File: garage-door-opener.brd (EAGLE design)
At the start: 54.3 x 47.6 mm, 17 parts, among them IC1 LM2575-3.3T, K1 RR1A, T1 BC547, U1 ESP8266, X2 Connector

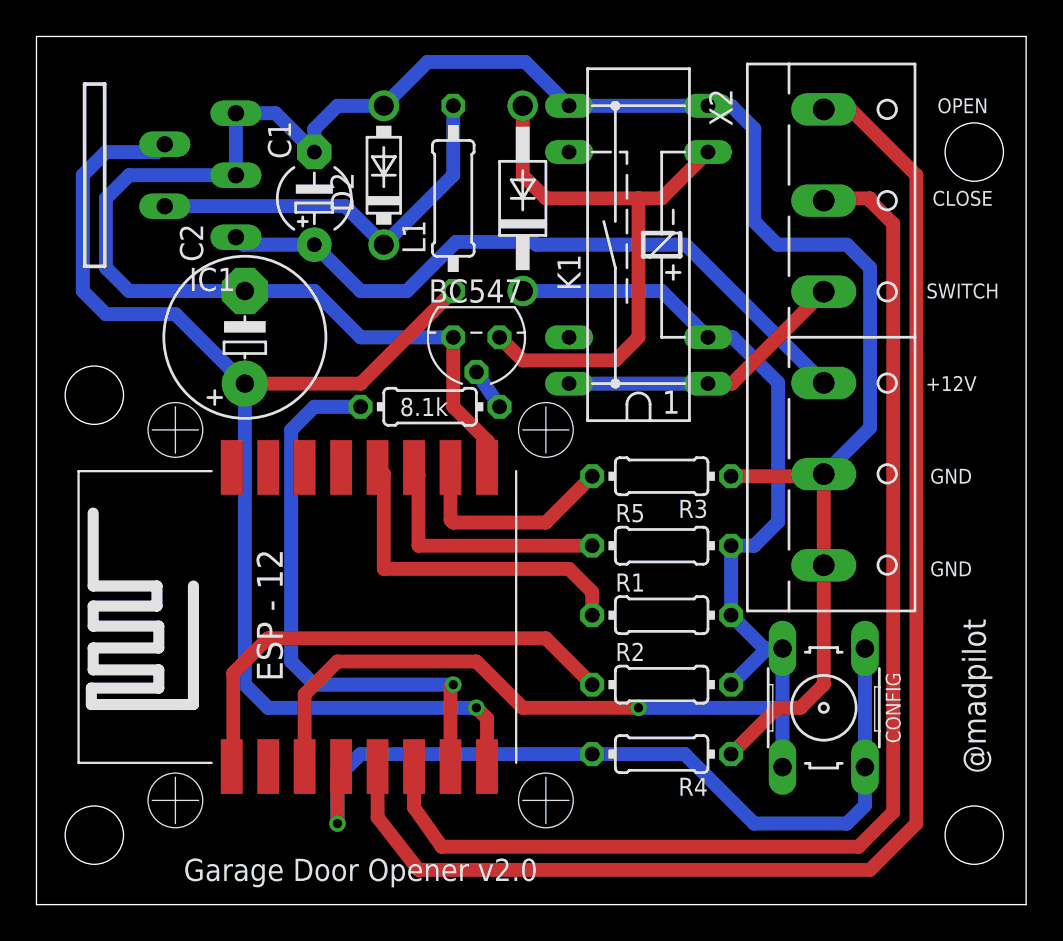
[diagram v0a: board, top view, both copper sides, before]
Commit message: Aligning resistors properly
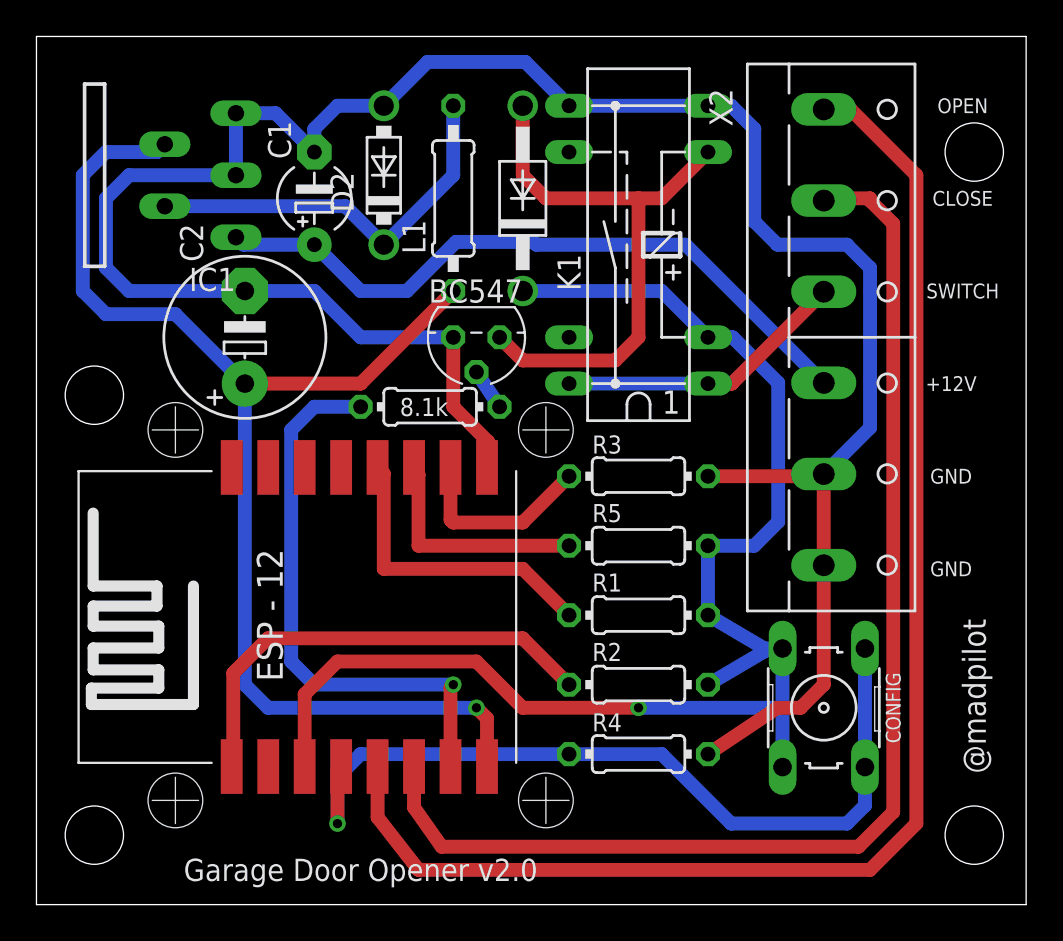
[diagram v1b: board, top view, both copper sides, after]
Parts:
- moved R1 1.27 mm to (33.0, 52.1)
- moved R2 1.27 mm to (33.0, 48.3)
- moved R3 1.27 mm to (33.0, 59.7)
- moved R4 1.27 mm to (33.0, 44.5)
- moved R5 1.27 mm to (33.0, 55.9)
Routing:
- net VCC: track 75.4 -> 78.7 mm
- net GND: track 125.2 -> 127.5 mm
- net N$7: track 18.9 -> 16.9 mm
- net N$8: track 26.7 -> 25.4 mm
- net N$6: track 11.8 -> 10.5 mm
- net N$13: track 13.9 -> 12.6 mm
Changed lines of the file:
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@@
 <attribute name="SPICEPREFIX" value="L" x="22.86" y="74.93" size="0.6096" layer="27" rot="R90" display="off"/>
 </element>
-<element name="R1" library="resistor" library_urn="urn:adsk.eagle:library:348" package="0204/7" package3d_urn="urn:adsk.eagle:package:25945/1" value="3k3" x="34.29" y="52.07"/>
-<element name="R2" library="resistor" library_urn="urn:adsk.eagle:library:348" package="0204/7" package3d_urn="urn:adsk.eagle:package:25945/1" value="3k3" x="34.29" y="48.26"/>
-<element name="R3" library="resistor" library_urn="urn:adsk.eagle:library:348" package="0204/7" package3d_urn="urn:adsk.eagle:package:25945/1" value="3k3" x="34.29" y="59.69" rot="R180"/>
+<element name="R1" library="resistor" library_urn="urn:adsk.eagle:library:348" package="0204/7" package3d_urn="urn:adsk.eagle:package:25945/1" value="3k3" x="33.02" y="52.07"/>
+<element name="R2" library="resistor" library_urn="urn:adsk.eagle:library:348" package="0204/7" package3d_urn="urn:adsk.eagle:package:25945/1" value="3k3" x="33.02" y="48.26"/>
+<element name="R3" library="resistor" library_urn="urn:adsk.eagle:library:348" package="0204/7" package3d_urn="urn:adsk.eagle:package:25945/1" value="3k3" x="33.02" y="59.69" smashed="yes" rot="R180">
+<attribute name="NAME" x="30.48" y="60.9346" size="0.9906" layer="25" ratio="10" rot="R180" align="top-right"/>
+<attribute name="VALUE" x="34.6456" y="60.1726" size="0.9906" layer="27" ratio="10" rot="R180"/>
+</element>
 <element name="K1" library="relay" library_urn="urn:adsk.eagle:library:339" package="RR1A" package3d_urn="urn:adsk.eagle:package:24316/1" value="RR1A" x="33.02" y="72.39" rot="R90">
 <attribute name="MF" value="" x="33.02" y="72.39" size="0.6096" layer="27" rot="R90" display="off"/>
@@
 <attribute name="OC_NEWARK" value="36M3542" x="43.18" y="46.99" size="0.6096" layer="27" rot="R90" display="off"/>
 </element>
-<element name="R4" library="resistor" library_urn="urn:adsk.eagle:library:348" package="0204/7" package3d_urn="urn:adsk.eagle:package:25945/1" value="3k3" x="34.29" y="44.45" rot="R180"/>
-<element name="R5" library="resistor" library_urn="urn:adsk.eagle:library:348" package="0204/7" package3d_urn="urn:adsk.eagle:package:25945/1" value="3k3" x="34.29" y="55.88"/>
+<element name="R4" library="resistor" library_urn="urn:adsk.eagle:library:348" package="0204/7" package3d_urn="urn:adsk.eagle:package:25945/1" value="3k3" x="33.02" y="44.45" smashed="yes" rot="R180">
+<attribute name="NAME" x="30.48" y="45.6946" size="0.9906" layer="25" ratio="10" rot="R180" align="top-right"/>
+<attribute name="VALUE" x="34.6456" y="44.9326" size="0.9906" layer="27" ratio="10" rot="R180"/>
+</element>
+<element name="R5" library="resistor" library_urn="urn:adsk.eagle:library:348" package="0204/7" package3d_urn="urn:adsk.eagle:package:25945/1" value="3k3" x="33.02" y="55.88" smashed="yes">
+<attribute name="NAME" x="30.48" y="57.1754" size="0.9906" layer="25" ratio="10"/>
+<attribute name="VALUE" x="31.3944" y="55.3974" size="0.9906" layer="27" ratio="10"/>
+</element>
 </elements>
 <signals>
@@
 <wire x1="15.24" y1="69.85" x2="17.78" y2="67.31" width="0.762" layer="16"/>
 <wire x1="17.78" y1="67.31" x2="22.86" y2="67.31" width="0.762" layer="16"/>
-<wire x1="38.1" y1="59.69" x2="43.18" y2="59.69" width="0.762" layer="1"/>
-<wire x1="38.1" y1="44.45" x2="40.64" y2="46.99" width="0.762" layer="1"/>
+<wire x1="36.83" y1="59.69" x2="43.18" y2="59.69" width="0.762" layer="1"/>
+<wire x1="36.83" y1="44.45" x2="40.64" y2="46.99" width="0.762" layer="1"/>
 <wire x1="40.64" y1="46.99" x2="41.91" y2="46.99" width="0.762" layer="1"/>
 <wire x1="41.91" y1="46.99" x2="43.18" y2="48.26" width="0.762" layer="1"/>
@@
 <contactref element="R5" pad="2"/>
 <wire x1="40.9194" y1="46.99" x2="40.9194" y2="43.7388" width="0.762" layer="16"/>
-<wire x1="38.1" y1="55.88" x2="38.1" y2="52.07" width="0.762" layer="16"/>
-<wire x1="38.1" y1="52.07" x2="39.9288" y2="50.2412" width="0.762" layer="16"/>
+<wire x1="36.83" y1="55.88" x2="36.83" y2="52.07" width="0.762" layer="16"/>
+<wire x1="36.83" y1="52.07" x2="39.9288" y2="50.2412" width="0.762" layer="16"/>
 <wire x1="39.9288" y1="50.2412" x2="40.9194" y2="50.2412" width="0.762" layer="16"/>
-<wire x1="38.1" y1="55.88" x2="39.37" y2="55.88" width="0.762" layer="16"/>
+<wire x1="36.83" y1="55.88" x2="39.37" y2="55.88" width="0.762" layer="16"/>
 <wire x1="40.68" y1="57.19" x2="40.68" y2="64.81" width="0.762" layer="16"/>
 <wire x1="39.37" y1="55.88" x2="40.68" y2="57.19" width="0.762" layer="16"/>
@@
 <via x="33.02" y="46.99" extent="1-16" drill="0.508"/>
 <wire x1="33.02" y1="46.99" x2="40.9194" y2="46.99" width="0.762" layer="16"/>
-<wire x1="38.1" y1="48.26" x2="39.9288" y2="50.0888" width="0.762" layer="16"/>
+<wire x1="36.83" y1="48.26" x2="39.9288" y2="50.0888" width="0.762" layer="16"/>
 <wire x1="39.9288" y1="50.0888" x2="39.9288" y2="50.2412" width="0.762" layer="16"/>
 </signal>
@@
 <contactref element="U1" pad="GPIO0"/>
 <contactref element="R1" pad="1"/>
-<wire x1="30.48" y1="52.07" x2="30.48" y2="53.34" width="0.762" layer="1"/>
-<wire x1="30.48" y1="53.34" x2="29.21" y2="54.61" width="0.762" layer="1"/>
-<wire x1="29.21" y1="54.61" x2="19.05" y2="54.61" width="0.762" layer="1"/>
+<wire x1="29.21" y1="52.07" x2="26.67" y2="54.61" width="0.762" layer="1"/>
+<wire x1="26.67" y1="54.61" x2="19.05" y2="54.61" width="0.762" layer="1"/>
 <wire x1="19.05" y1="54.61" x2="19.05" y2="59.83" width="0.762" layer="1"/>
 <wire x1="19.05" y1="59.83" x2="18.71" y2="60.17" width="0.762" layer="1"/>
@@
 <wire x1="10.795" y1="44.45" x2="10.795" y2="48.895" width="0.762" layer="1"/>
 <wire x1="10.795" y1="48.895" x2="12.7" y2="50.8" width="0.762" layer="1"/>
-<wire x1="12.7" y1="50.8" x2="27.94" y2="50.8" width="0.762" layer="1"/>
-<wire x1="27.94" y1="50.8" x2="30.48" y2="48.26" width="0.762" layer="1"/>
+<wire x1="12.7" y1="50.8" x2="26.67" y2="50.8" width="0.762" layer="1"/>
+<wire x1="26.67" y1="50.8" x2="29.21" y2="48.26" width="0.762" layer="1"/>
 </signal>
 <signal name="N$9">
@@
 <wire x1="16.51" y1="43.57" x2="16.71" y2="43.77" width="0.762" layer="1"/>
 <wire x1="45.4406" y1="50.2412" x2="45.4406" y2="43.7388" width="0.762" layer="16"/>
-<wire x1="30.48" y1="44.45" x2="35.56" y2="44.45" width="0.762" layer="16"/>
-<wire x1="35.56" y1="44.45" x2="39.37" y2="40.64" width="0.762" layer="16"/>
-<wire x1="39.37" y1="40.64" x2="44.45" y2="40.64" width="0.762" layer="16"/>
+<wire x1="29.21" y1="44.45" x2="34.29" y2="44.45" width="0.762" layer="16"/>
+<wire x1="34.29" y1="44.45" x2="38.1" y2="40.64" width="0.762" layer="16"/>
+<wire x1="38.1" y1="40.64" x2="44.45" y2="40.64" width="0.762" layer="16"/>
 <wire x1="17.78" y1="44.45" x2="16.51" y2="43.18" width="0.762" layer="16"/>
 <wire x1="16.51" y1="43.18" x2="16.51" y2="40.64" width="0.762" layer="16"/>
-<wire x1="30.48" y1="44.45" x2="17.78" y2="44.45" width="0.762" layer="16"/>
+<wire x1="29.21" y1="44.45" x2="17.78" y2="44.45" width="0.762" layer="16"/>
 </signal>
 <signal name="N$6">
 <contactref element="U1" pad="GPIO15"/>
 <contactref element="R3" pad="2"/>
-<wire x1="30.48" y1="59.69" x2="27.94" y2="57.15" width="0.762" layer="1"/>
+<wire x1="29.21" y1="59.69" x2="26.67" y2="57.15" width="0.762" layer="1"/>
 <wire x1="22.86" y1="57.15" x2="22.71" y2="57.3" width="0.762" layer="1"/>
 <wire x1="22.71" y1="57.3" x2="22.71" y2="60.17" width="0.762" layer="1"/>
-<wire x1="27.94" y1="57.15" x2="22.86" y2="57.15" width="0.762" layer="1"/>
+<wire x1="26.67" y1="57.15" x2="22.86" y2="57.15" width="0.762" layer="1"/>
 </signal>
 <signal name="N$13">
 <contactref element="U1" pad="GPIO2"/>
 <contactref element="R5" pad="1"/>
-<wire x1="30.48" y1="55.88" x2="20.955" y2="55.88" width="0.762" layer="1"/>
+<wire x1="29.21" y1="55.88" x2="20.955" y2="55.88" width="0.762" layer="1"/>
 <wire x1="20.955" y1="59.78" x2="20.71" y2="60.17" width="0.762" layer="1"/>
 <wire x1="20.955" y1="55.88" x2="20.955" y2="59.78" width="0.762" layer="1"/>

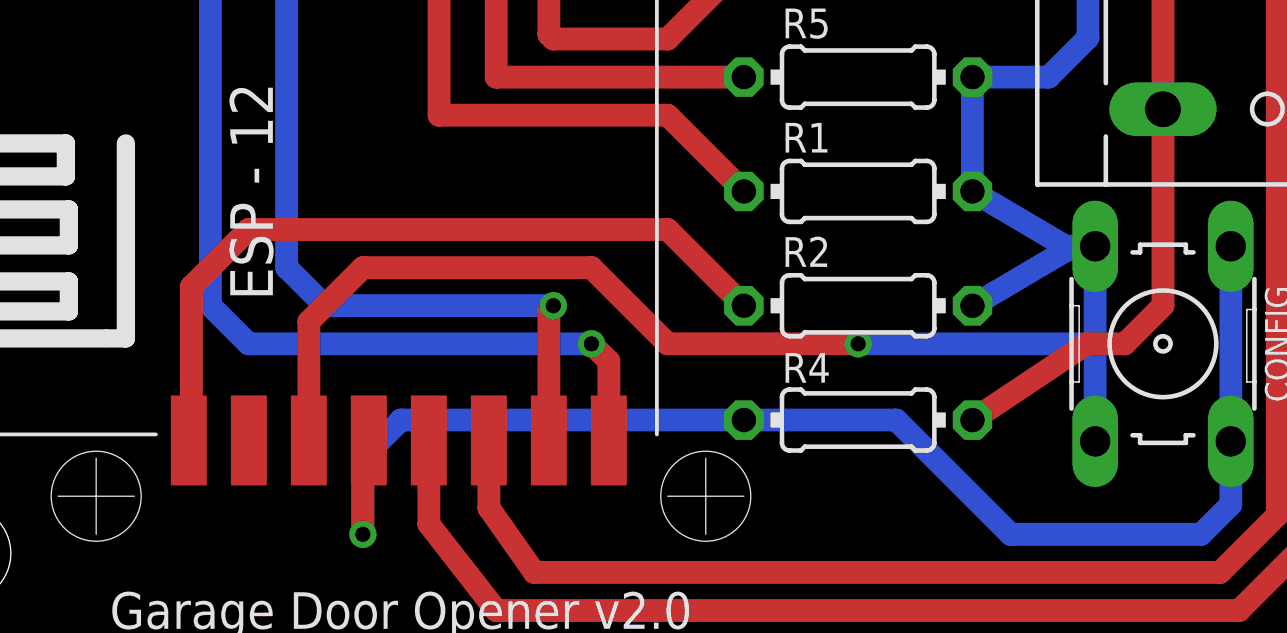
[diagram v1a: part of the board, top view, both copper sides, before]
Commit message: Cleaning out some routes. Eliminating a via
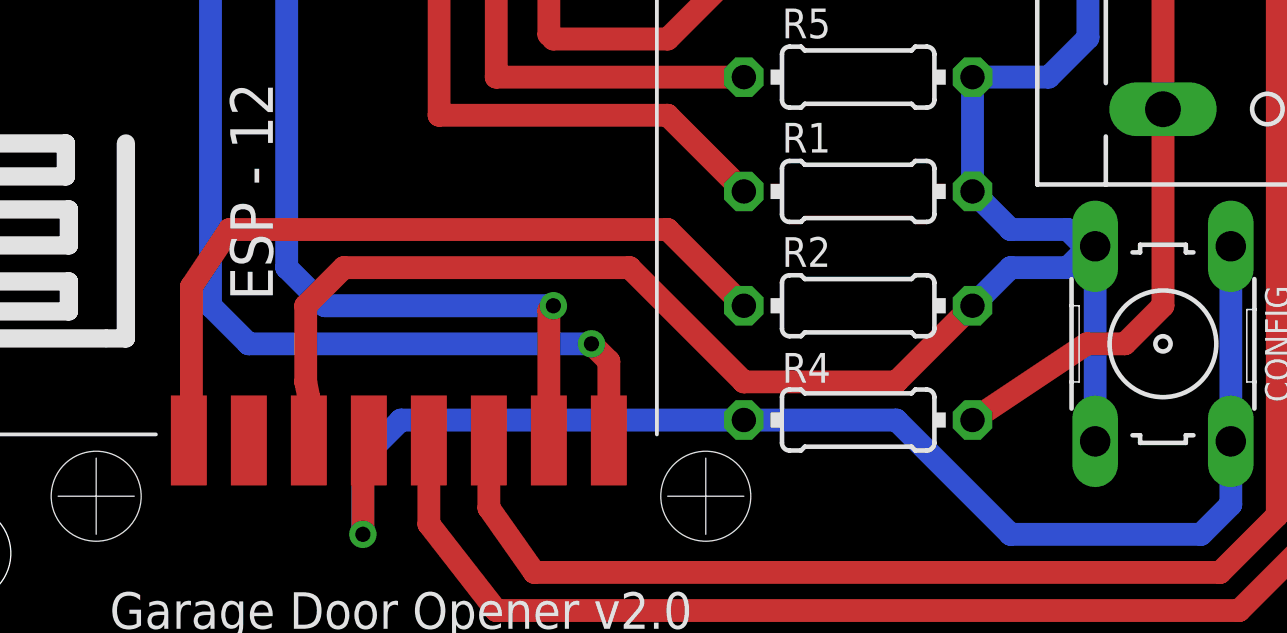
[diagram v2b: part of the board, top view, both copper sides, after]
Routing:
- net VCC: track 78.7 -> 78.1 mm, vias 1 -> 0
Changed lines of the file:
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@@
 <contactref element="S1" pad="1"/>
 <contactref element="S1" pad="2"/>
-<wire x1="40.9194" y1="50.2412" x2="40.9194" y2="46.99" width="0.762" layer="16"/>
 <contactref element="U1" pad="CH_PD"/>
 <contactref element="R5" pad="2"/>
-<wire x1="40.9194" y1="46.99" x2="40.9194" y2="43.7388" width="0.762" layer="16"/>
+<wire x1="40.9194" y1="50.2412" x2="40.9194" y2="43.7388" width="0.762" layer="16"/>
 <wire x1="36.83" y1="55.88" x2="36.83" y2="52.07" width="0.762" layer="16"/>
-<wire x1="36.83" y1="52.07" x2="39.9288" y2="50.2412" width="0.762" layer="16"/>
-<wire x1="39.9288" y1="50.2412" x2="40.9194" y2="50.2412" width="0.762" layer="16"/>
 <wire x1="36.83" y1="55.88" x2="39.37" y2="55.88" width="0.762" layer="16"/>
 <wire x1="40.68" y1="57.19" x2="40.68" y2="64.81" width="0.762" layer="16"/>
 <wire x1="39.37" y1="55.88" x2="40.68" y2="57.19" width="0.762" layer="16"/>
-<wire x1="24.13" y1="49.53" x2="26.67" y2="46.99" width="0.762" layer="1"/>
-<wire x1="24.13" y1="49.53" x2="16.51" y2="49.53" width="0.762" layer="1"/>
-<wire x1="16.51" y1="49.53" x2="14.71" y2="47.73" width="0.762" layer="1"/>
-<wire x1="14.71" y1="47.73" x2="14.71" y2="43.77" width="0.762" layer="1"/>
 <contactref element="R2" pad="2"/>
-<wire x1="26.67" y1="46.99" x2="33.02" y2="46.99" width="0.762" layer="1"/>
-<via x="33.02" y="46.99" extent="1-16" drill="0.508"/>
-<wire x1="33.02" y1="46.99" x2="40.9194" y2="46.99" width="0.762" layer="16"/>
-<wire x1="36.83" y1="48.26" x2="39.9288" y2="50.0888" width="0.762" layer="16"/>
-<wire x1="39.9288" y1="50.0888" x2="39.9288" y2="50.2412" width="0.762" layer="16"/>
+<wire x1="14.71" y1="43.77" x2="14.71" y2="45.19" width="0.762" layer="1"/>
+<wire x1="25.4" y1="49.53" x2="29.21" y2="45.72" width="0.762" layer="1"/>
+<wire x1="29.21" y1="45.72" x2="34.29" y2="45.72" width="0.762" layer="1"/>
+<wire x1="34.29" y1="45.72" x2="36.83" y2="48.26" width="0.762" layer="1"/>
+<wire x1="36.83" y1="52.07" x2="38.1" y2="50.8" width="0.762" layer="16"/>
+<wire x1="38.1" y1="50.8" x2="40.005" y2="50.8" width="0.762" layer="16"/>
+<wire x1="40.005" y1="50.8" x2="40.5638" y2="50.2412" width="0.762" layer="16"/>
+<wire x1="40.5638" y1="50.2412" x2="40.9194" y2="50.2412" width="0.762" layer="16"/>
+<wire x1="36.83" y1="48.26" x2="38.1" y2="49.53" width="0.762" layer="16"/>
+<wire x1="38.1" y1="49.53" x2="40.005" y2="49.53" width="0.762" layer="16"/>
+<wire x1="40.005" y1="49.53" x2="40.7162" y2="50.2412" width="0.762" layer="16"/>
+<wire x1="40.7162" y1="50.2412" x2="40.9194" y2="50.2412" width="0.762" layer="16"/>
+<wire x1="14.71" y1="45.19" x2="14.605" y2="45.72" width="0.762" layer="1"/>
+<wire x1="14.605" y1="45.72" x2="14.605" y2="48.26" width="0.762" layer="1"/>
+<wire x1="14.605" y1="48.26" x2="15.875" y2="49.53" width="0.762" layer="1"/>
+<wire x1="15.875" y1="49.53" x2="25.4" y2="49.53" width="0.762" layer="1"/>
 </signal>
 <signal name="N$4">
@@
 <wire x1="10.75" y1="43.77" x2="10.795" y2="44.45" width="0.762" layer="1"/>
 <wire x1="10.795" y1="44.45" x2="10.795" y2="48.895" width="0.762" layer="1"/>
-<wire x1="10.795" y1="48.895" x2="12.7" y2="50.8" width="0.762" layer="1"/>
-<wire x1="12.7" y1="50.8" x2="26.67" y2="50.8" width="0.762" layer="1"/>
+<wire x1="10.795" y1="48.895" x2="12.065" y2="50.8" width="0.762" layer="1"/>
+<wire x1="12.065" y1="50.8" x2="26.67" y2="50.8" width="0.762" layer="1"/>
 <wire x1="26.67" y1="50.8" x2="29.21" y2="48.26" width="0.762" layer="1"/>
 </signal>
